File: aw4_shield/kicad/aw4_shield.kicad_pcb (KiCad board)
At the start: 2 copper layers, 145 x 100 mm, 78 parts, among them J1 J1 +12V / PGND, J2 J2 SOL1-3 / TCU1-3, J3 J3 UP DOWN READY LOCKUP, J5 J5 Nextion +5V GND RX TX, J6 J6 rezerva, K1 G5LE-1 12V SPDT, K2 G5LE-1 12V SPDT, K3 G5LE-1 12V SPDT, Q1 IRF4905, Q2 BC337, Q3 IRF9540N, Q4 IRF9540N, Q5 IRF9540N, U1 TSR 1-2450 (12V->5V 1A), U2 Arduino Nano, U3 PC817, U4 PC817, U5 PC817, U6 PC817

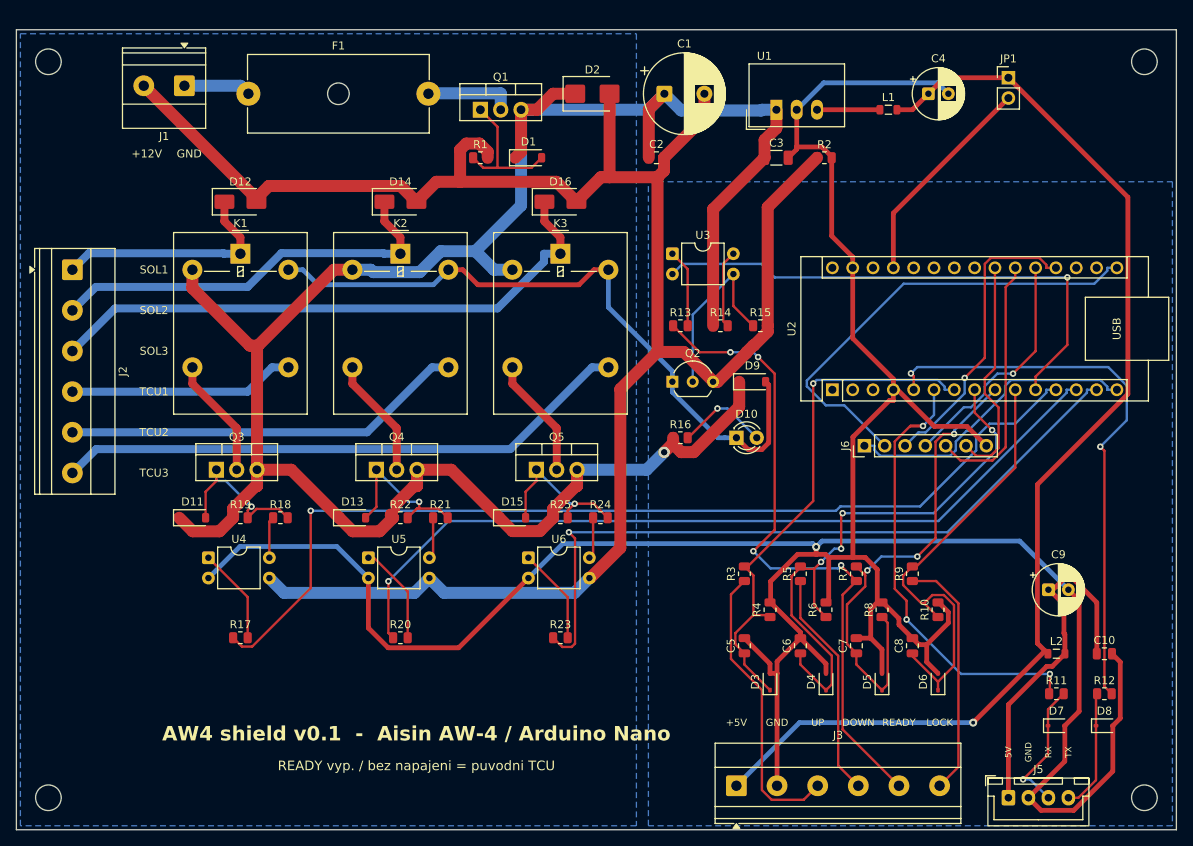
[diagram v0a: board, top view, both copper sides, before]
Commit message: AW4 shield v0.3: all through-hole parts, 100x100 mm board, values on silkscreen, order list
- every SMD part replaced by a through-hole one (vertical resistors/diodes,
  P6KE27A, 1N4007, BZX55 zeners, disc/radial caps, TR5 fuse holder)
- re-placed and re-routed on 100x100 mm; ERC/DRC/parity clean in KiCad 10.0.6
- silkscreen prints what to fit (value) at each part; references on F.Fab
- bom_objednavka.xlsx: order list with board-count multiplier + assembly order
- interactive BOM (docs/aw4_shield_ibom.html) and assembly drawing PDF

Co-Authored-By: Claude Opus 5.5 <noreply@anthropic.com>
Claude-Session: https://claude.ai/code/session_01QHDQqfFe1juWLgZ1EWa6E5
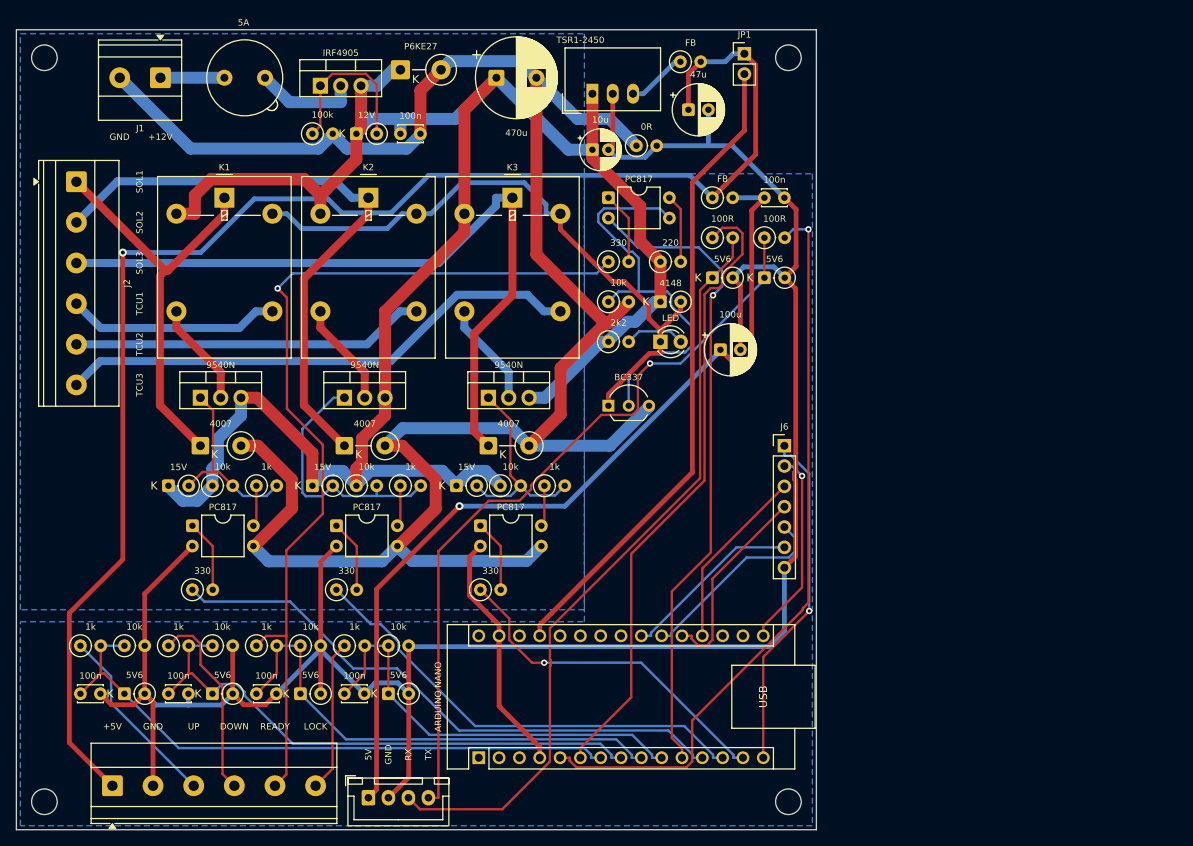
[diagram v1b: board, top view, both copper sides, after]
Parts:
- C10, C2, C5, C6, C7, C8: footprint Capacitor_SMD:C_0805_2012Metric -> Capacitor_THT:C_Disc_D3.0mm_W2.0mm_P2.50mm
- C3: footprint Capacitor_SMD:C_1206_3216Metric -> Capacitor_THT:CP_Radial_D5.0mm_P2.00mm
- D1: value BZT52C12 -> BZX55C12; footprint Diode_SMD:D_SOD-123 -> Diode_THT:D_DO-35_SOD27_P2.54mm_Vertical_CathodeUp
- D11, D13, D15: value BZT52C15 -> BZX55C15; footprint Diode_SMD:D_SOD-123 -> Diode_THT:D_DO-35_SOD27_P2.54mm_Vertical_CathodeUp
- D12, D14, D16: value SS34 -> 1N4007; footprint Diode_SMD:D_SMA -> Diode_THT:D_DO-41_SOD81_P5.08mm_Vertical_CathodeUp
- D2: value SMBJ24A -> P6KE27A; footprint Diode_SMD:D_SMB -> Diode_THT:D_DO-15_P5.08mm_Vertical_CathodeUp
- D3, D4, D5, D6, D7, D8: value PESD5V0S1BL -> BZX55C5V6; footprint Diode_SMD:D_SOD-323 -> Diode_THT:D_DO-35_SOD27_P2.54mm_Vertical_CathodeUp
- D9: value 1N4148W -> 1N4148; footprint Diode_SMD:D_SOD-123 -> Diode_THT:D_DO-35_SOD27_P2.54mm_Vertical_CathodeUp
- F1: footprint Fuse:Fuseholder_Cylinder-5x20mm_Schurter_0031_8201_Horizontal_Open -> Fuse:Fuseholder_TR5_Littelfuse_No560_No460
- L1, L2: footprint Inductor_SMD:L_0805_2012Metric -> Resistor_THT:R_Axial_DIN0207_L6.3mm_D2.5mm_P2.54mm_Vertical
- R1, R10, R11, R12, R13, R14, R15, R16, R17, R18, R19, R2, R20, R21, R22, R23, R24, R25, R3, R4, R5, R6, R7, R8, R9: footprint Resistor_SMD:R_0805_2012Metric -> Resistor_THT:R_Axial_DIN0207_L6.3mm_D2.5mm_P2.54mm_Vertical
- moved R3 83.5 mm to (108.0, 177.0), turned to 0 degrees
- moved C5 83.2 mm to (108.0, 183.0), turned to 0 degrees
- moved R4 80.8 mm to (113.5, 177.0), turned to 0 degrees
- moved D3 80.7 mm to (113.5, 183.0), turned to 0 degrees
- moved J5 80.0 mm to (144.0, 196.0)
- moved R5 79.5 mm to (119.0, 177.0), turned to 0 degrees
- moved C6 79.2 mm to (119.0, 183.0), turned to 0 degrees
- moved J3 78.0 mm to (112.0, 194.5)
- moved R6 76.8 mm to (124.5, 177.0), turned to 0 degrees
- moved D4 76.7 mm to (124.5, 183.0), turned to 0 degrees
- moved R7 75.5 mm to (130.0, 177.0), turned to 0 degrees
- moved C7 75.2 mm to (130.0, 183.0), turned to 0 degrees
- moved R8 72.8 mm to (135.5, 177.0), turned to 0 degrees
- moved D5 72.7 mm to (135.5, 183.0), turned to 0 degrees
- moved R9 71.6 mm to (141.0, 177.0), turned to 0 degrees
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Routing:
- net /DISP_TX: track 15.2 -> 94.9 mm, vias 0 -> 1
- net /DISP_RX: track 16.9 -> 95.8 mm, vias 1 -> 0
- net /GND: track 385.4 -> 318.6 mm, vias 1 -> 0
- net /+5V_DISP: track 44.3 -> 110.9 mm, vias 0 -> 1
- net /NANO_5V: track 27.2 -> 80.8 mm
- net /SOL1_CTRL: track 123.5 -> 72.9 mm, vias 1 -> 0
- net /SOL3_CTRL: track 91.2 -> 43.3 mm
- net /SOL2_CTRL: track 103.4 -> 57.7 mm, vias 1 -> 0
- net /+5V: track 144.6 -> 185.3 mm
- net /D13: track 58.3 -> 24.7 mm, vias 0 -> 1
- net /READY_IN: track 82.5 -> 113.9 mm, vias 4 -> 1
- net /Q4_B: track 23.0 -> 50.9 mm
- net /SOL2_OUT: track 51.3 -> 75.9 mm
- net /SOL1_OUT: track 29.2 -> 52.3 mm
- net /D2_UART_RX: track 70.9 -> 93.5 mm, vias 2 -> 1
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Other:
- board size 145 x 100 mm -> 100 x 100 mm
- board text added: "AW4 shield v0.3 (THT, 100x100)"
- board text added: "Aisin AW-4 / Arduino Nano / Nextion"
- board text removed: "AW4 shield v0.1 - Aisin AW-4 / Arduino Nano"

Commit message: AW4 shield: R14 220R -> 2k2 (opto/base current limit), design review notes
With a high-CTR PC817 the relay driver could push ~50 mA through R14 (0.55 W
in a 0.25 W resistor). 2k2 limits base current to ~5 mA, still enough for
the 90 mA relay coils with BC337.

Co-Authored-By: Claude Opus 5.5 <noreply@anthropic.com>
Claude-Session: https://claude.ai/code/session_01QHDQqfFe1juWLgZ1EWa6E5
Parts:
- R14: value 220 -> 2k2

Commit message: AW4 shield: DigiKey BOM (CSV for BOM Manager + xlsx sheet), C4/C9 100uF 16V
- digikey_bom.csv with manufacturer part numbers for every part, matched by
  DigiKey BOM Manager; DigiKey sheet in bom_objednavka.xlsx scales with board count
- C4 47uF/10V -> 100uF/16V so both 6.3 mm caps are the same part and match
  the footprint; board regenerated, ERC/DRC/parity still clean

Co-Authored-By: Claude Opus 5.5 <noreply@anthropic.com>
Claude-Session: https://claude.ai/code/session_01QHDQqfFe1juWLgZ1EWa6E5
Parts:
- C4: value 47uF 10V -> 100uF 16V
- C9: value 100uF 10V -> 100uF 16V
